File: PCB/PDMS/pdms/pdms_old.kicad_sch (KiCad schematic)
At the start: 46 parts, among them IC19 STM32L496ZGT6, IC20 AT25SF128A-SHB-T, J1 DBG, J2 6473427-1, Y1 48Mhz, Y2 32KHz

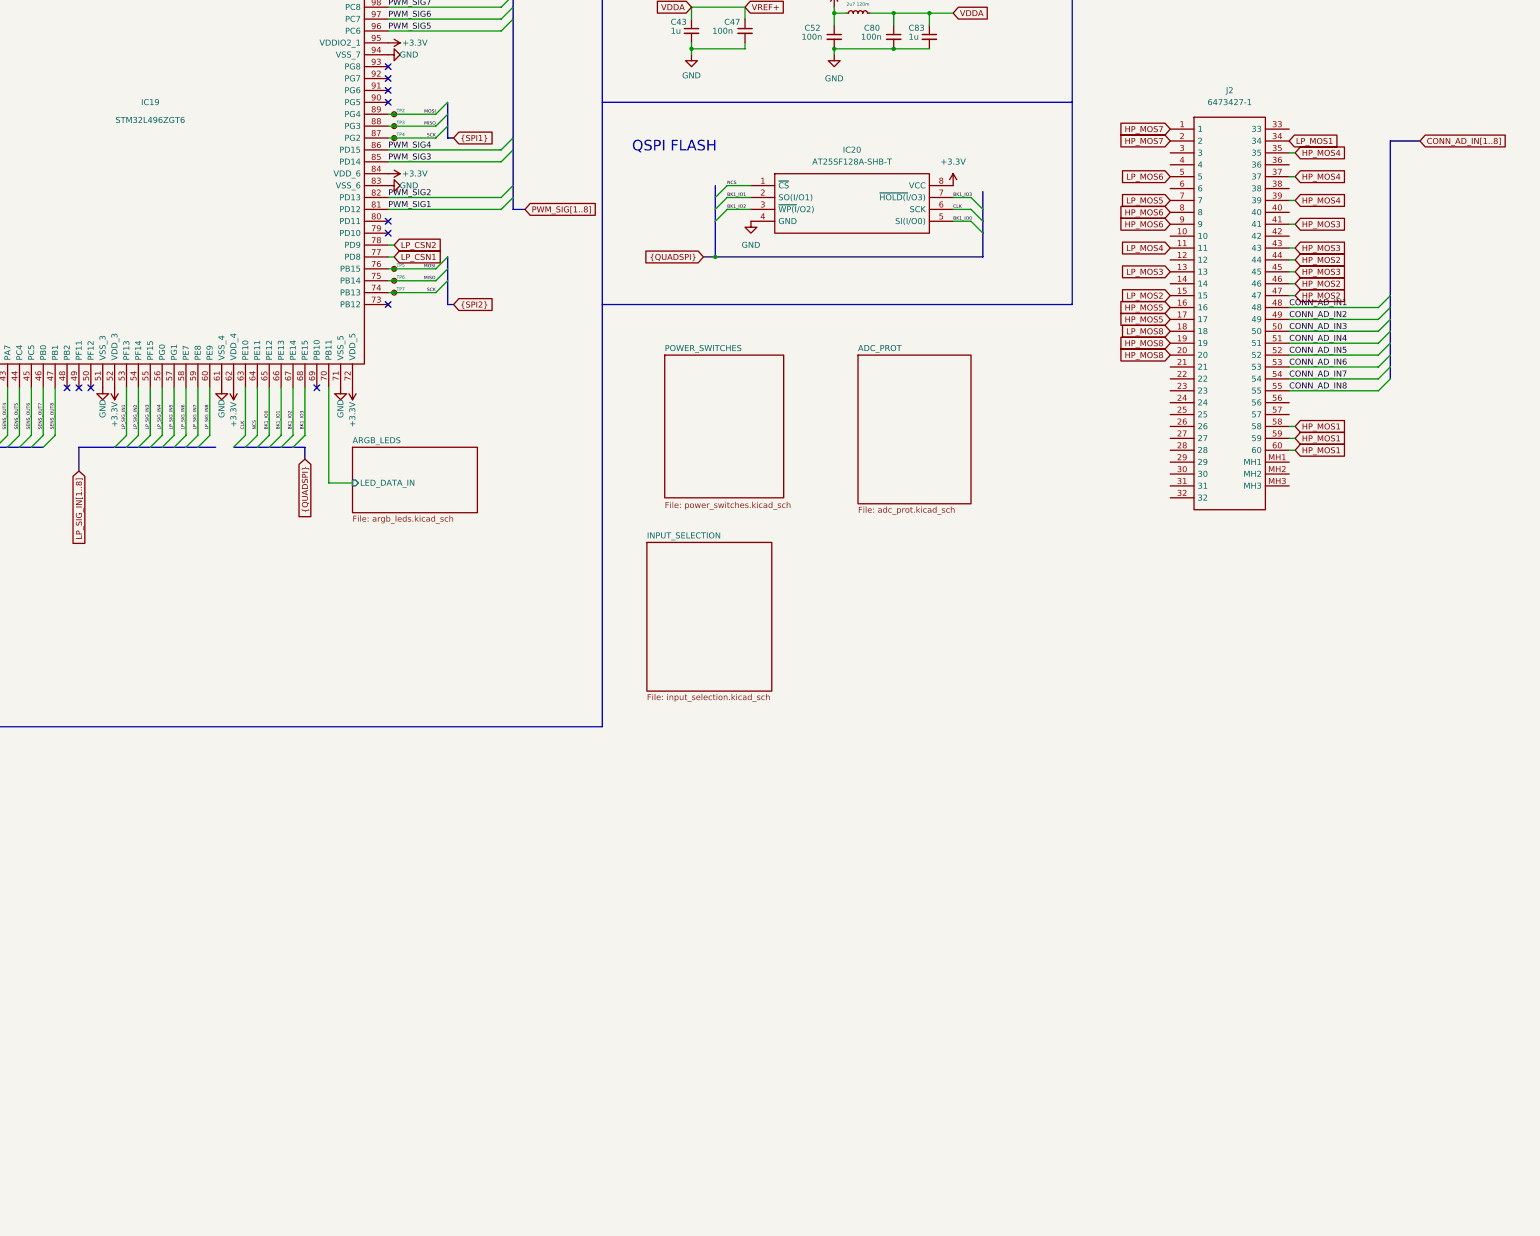
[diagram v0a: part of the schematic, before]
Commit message: Added Low power traces layout '4mm'
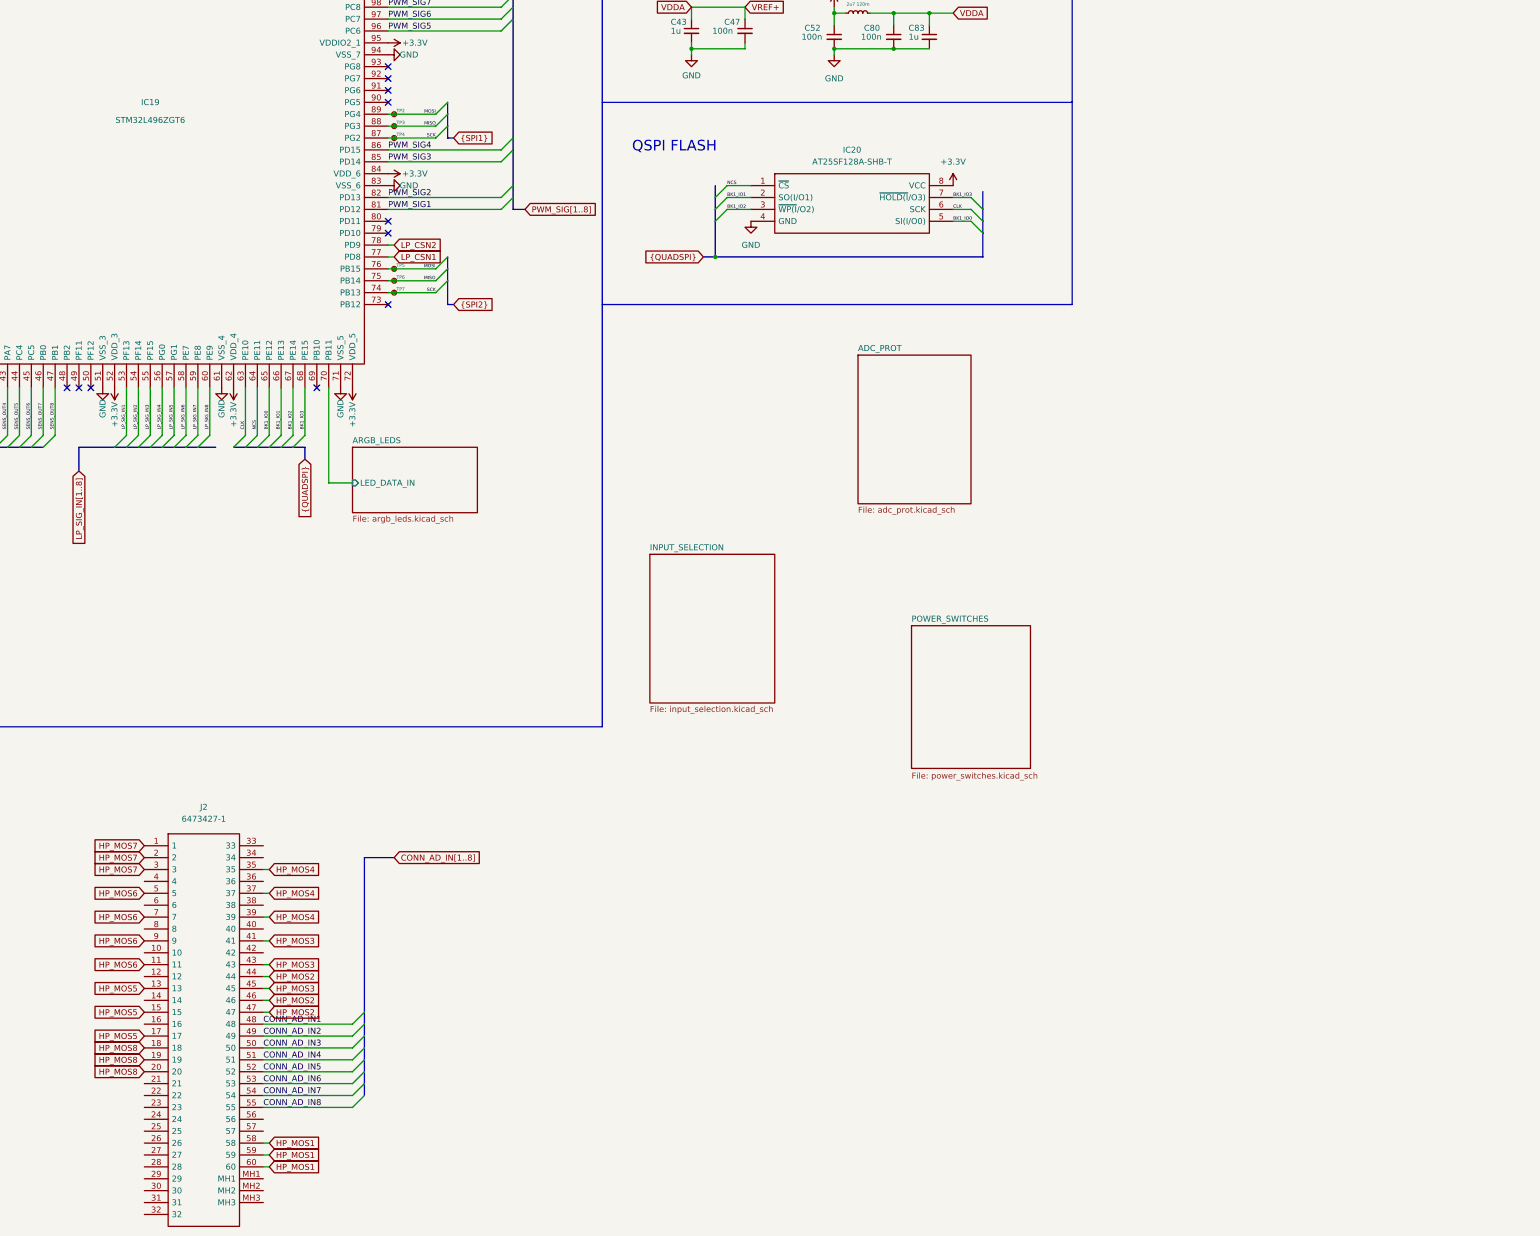
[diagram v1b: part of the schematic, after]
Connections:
- net LP_MOS2 is gone; now on net HP_MOS5: J2.15
- net LP_MOS3 is gone; now on net HP_MOS5: J2.13
- net LP_MOS4 is gone; now on net HP_MOS6: J2.11
- net LP_MOS5 is gone; now on net HP_MOS6: J2.7
- net LP_MOS6 is gone; now on net HP_MOS6: J2.5
- net LP_MOS8 is gone; now on net HP_MOS8: J2.18
- net HP_MOS5: no longer J2.16
- net HP_MOS6: no longer J2.8
- net HP_MOS7: now also J2.3
- net LP_MOS1: no longer names the net of J2.34
